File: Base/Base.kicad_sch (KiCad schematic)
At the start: 33 parts, among them J1 USB_C_Receptacle_USB2.0_16P, J10 JST_switch_1, J11 JST_switch_2, J12 Conn_touch_1, J13 Conn_touch_2, J2 JST_battery, J3 JST_header, J4 JST_speaker, J5 JST_debug_swd, J6 JST_debug_serial, J7 Conn_speaker_sd, J8 Conn_speaker_gain, J9 Conn_speaker_gnd, SW1 SW_power, U1 MCP73831-2-OT, U2 MAX98357A

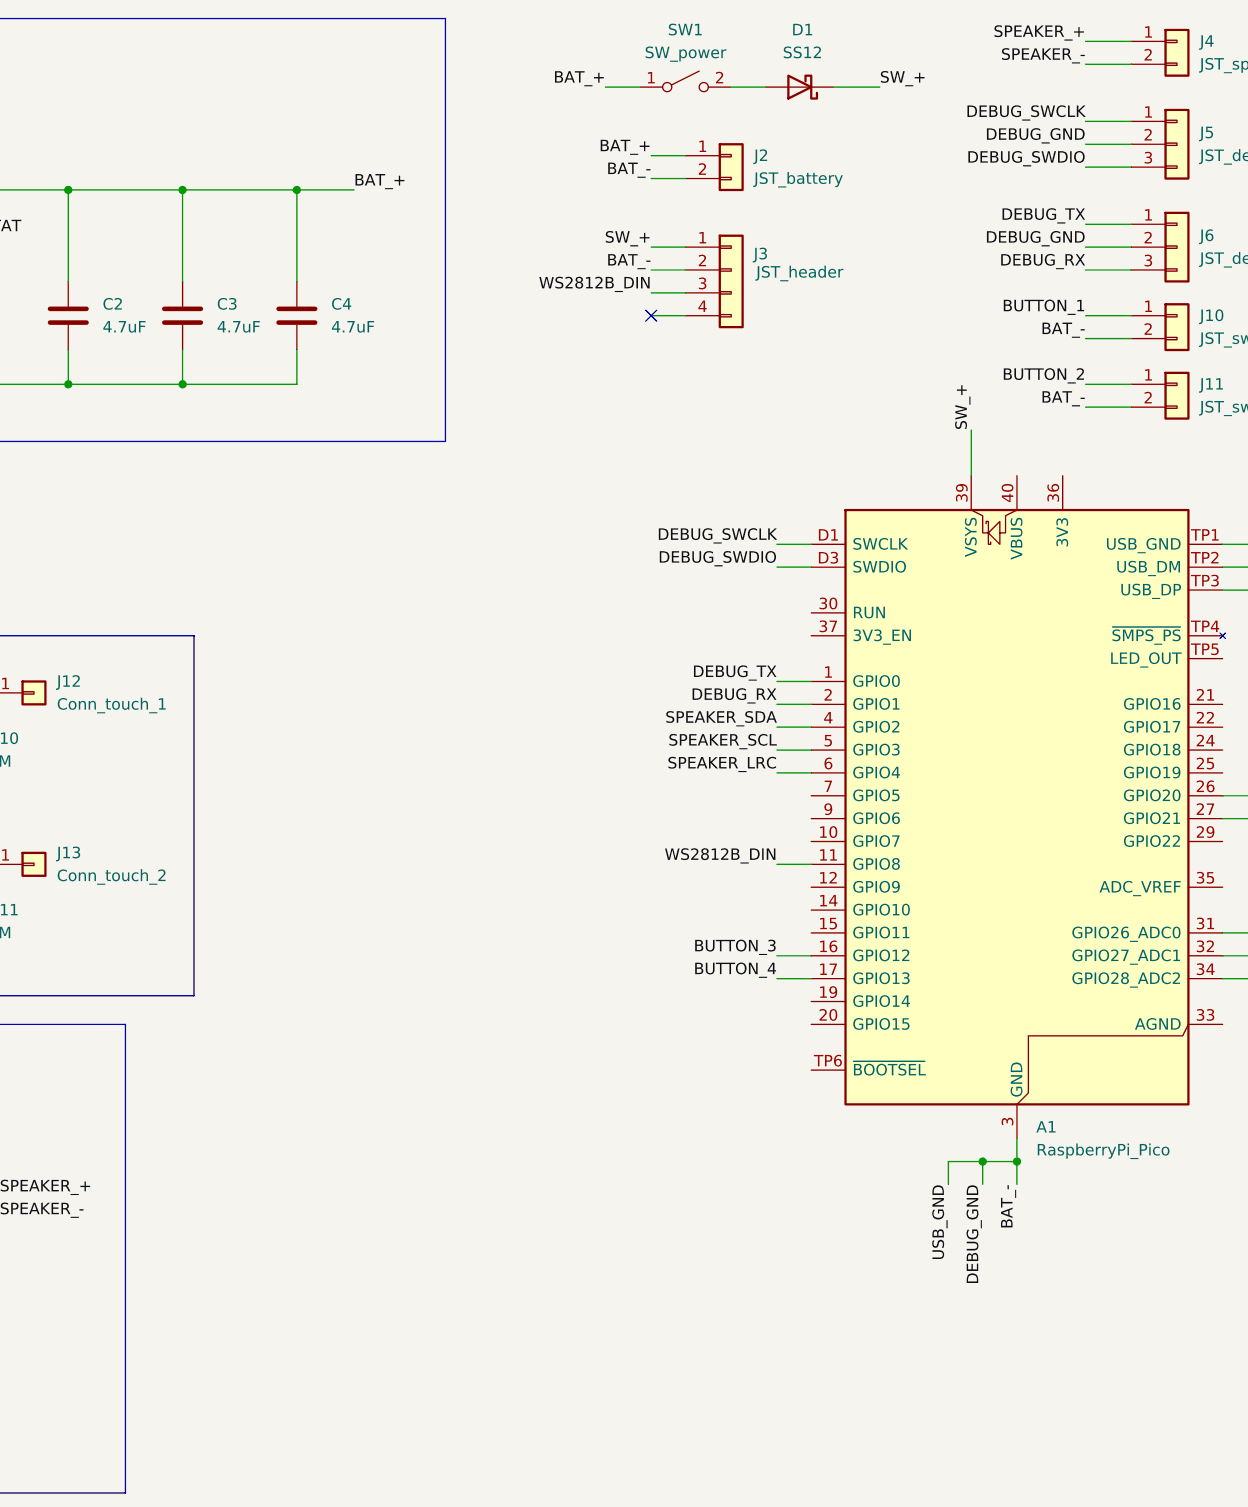
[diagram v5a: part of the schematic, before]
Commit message: Change switch to JST, fix polarity of battery connector, add power transistors for better LED off capability
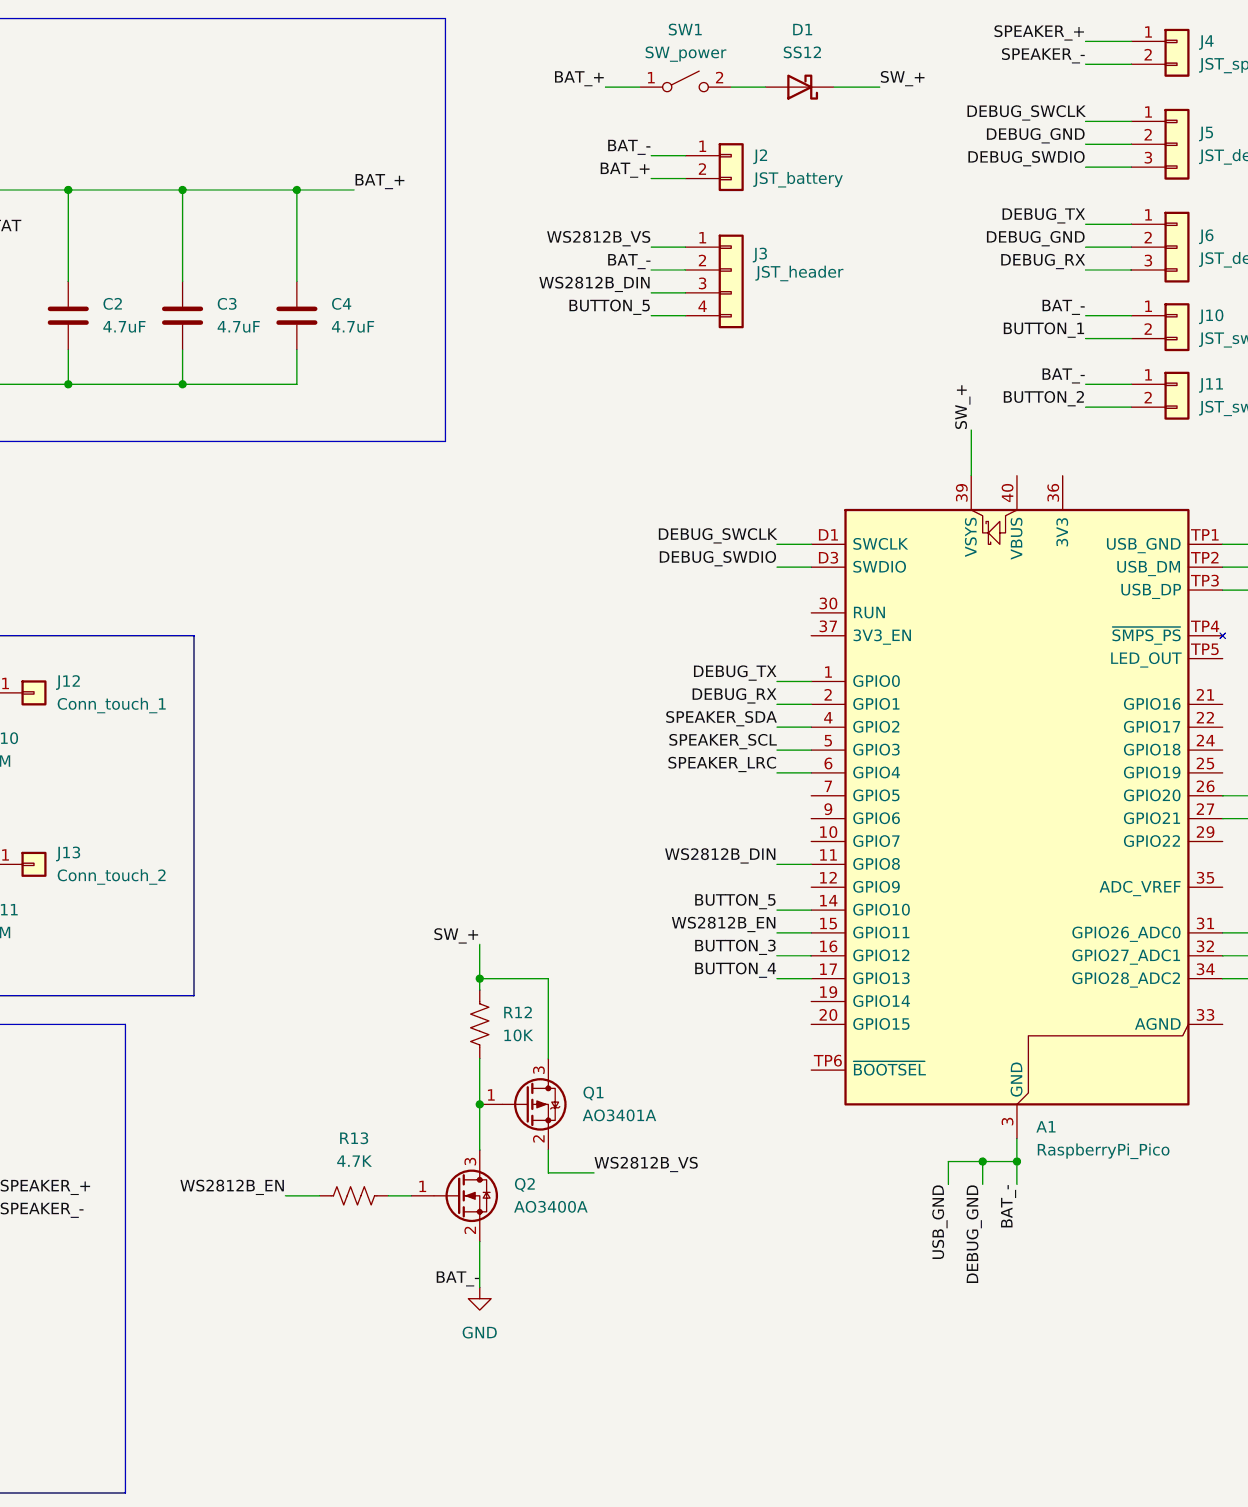
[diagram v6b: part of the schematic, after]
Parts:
- added Q1: AO3401A, Package_TO_SOT_SMD:SOT-23, symbol Transistor_FET:AO3401A
- added Q2: AO3400A, Package_TO_SOT_SMD:SOT-23, symbol Transistor_FET:AO3400A
- added R12: 10K, Resistor_SMD:R_0603_1608Metric_Pad0.98x0.95mm_HandSolder, symbol Device:R_US
- added R13: 4.7K, Resistor_SMD:R_0603_1608Metric_Pad0.98x0.95mm_HandSolder, symbol Device:R_US
- J10, J11: footprint Connector_JST:JST_SH_SM02B-SRSS-TB_1x02-1MP_P1.00mm_Horizontal -> Connector_JST:JST_SH_BM02B-SRSS-TB_1x02-1MP_P1.00mm_Vertical
- J2: footprint Connector_JST:JST_SH_SM02B-SRSS-TB_1x02-1MP_P1.00mm_Horizontal -> Connector_JST:JST_PH_B2B-PH-SM4-TB_1x02-1MP_P2.00mm_Vertical
- J4: footprint Connector_JST:JST_PH_B2B-PH-SM4-TB_1x02-1MP_P2.00mm_Vertical -> Connector_JST:JST_SH_BM02B-SRSS-TB_1x02-1MP_P1.00mm_Vertical
- SW1: footprint Button_Switch_SMD:SW_SPST_B3U-3000P -> Connector_JST:JST_SH_BM02B-SRSS-TB_1x02-1MP_P1.00mm_Vertical
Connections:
- net BAT_+: now also J2.2 (Pin_2); no longer J2.1 (Pin_1)
- net BUTTON_1: now also J10.2 (Pin_2); no longer J10.1 (Pin_1)
- net BUTTON_2: now also J11.2 (Pin_2); no longer J11.1 (Pin_1)
- net SW_+: now also Q1.3 (D), R12.1; no longer J3.1 (Pin_1)
- net BUTTON_5: now reaches A1.14 (GPIO10)
- net BUTTON_5: now also J3.4 (Pin_4)
- net WS2812B_EN: now reaches A1.15 (GPIO11)
- net WS2812B_EN: now also R13.1
- net BAT_- renamed GND
- net GND: now also J10.1 (Pin_1), J11.1 (Pin_1), J2.1 (Pin_1), Q2.2 (S); no longer J10.2 (Pin_2), J11.2 (Pin_2), J2.2 (Pin_2)
- new net: Q1.1 (G), Q2.3 (D), R12.2
- new net: Q2.1 (G), R13.2
- new net WS2812B_VS: J3.1 (Pin_1), Q1.2 (S)
- no-connect marks 4 -> 3

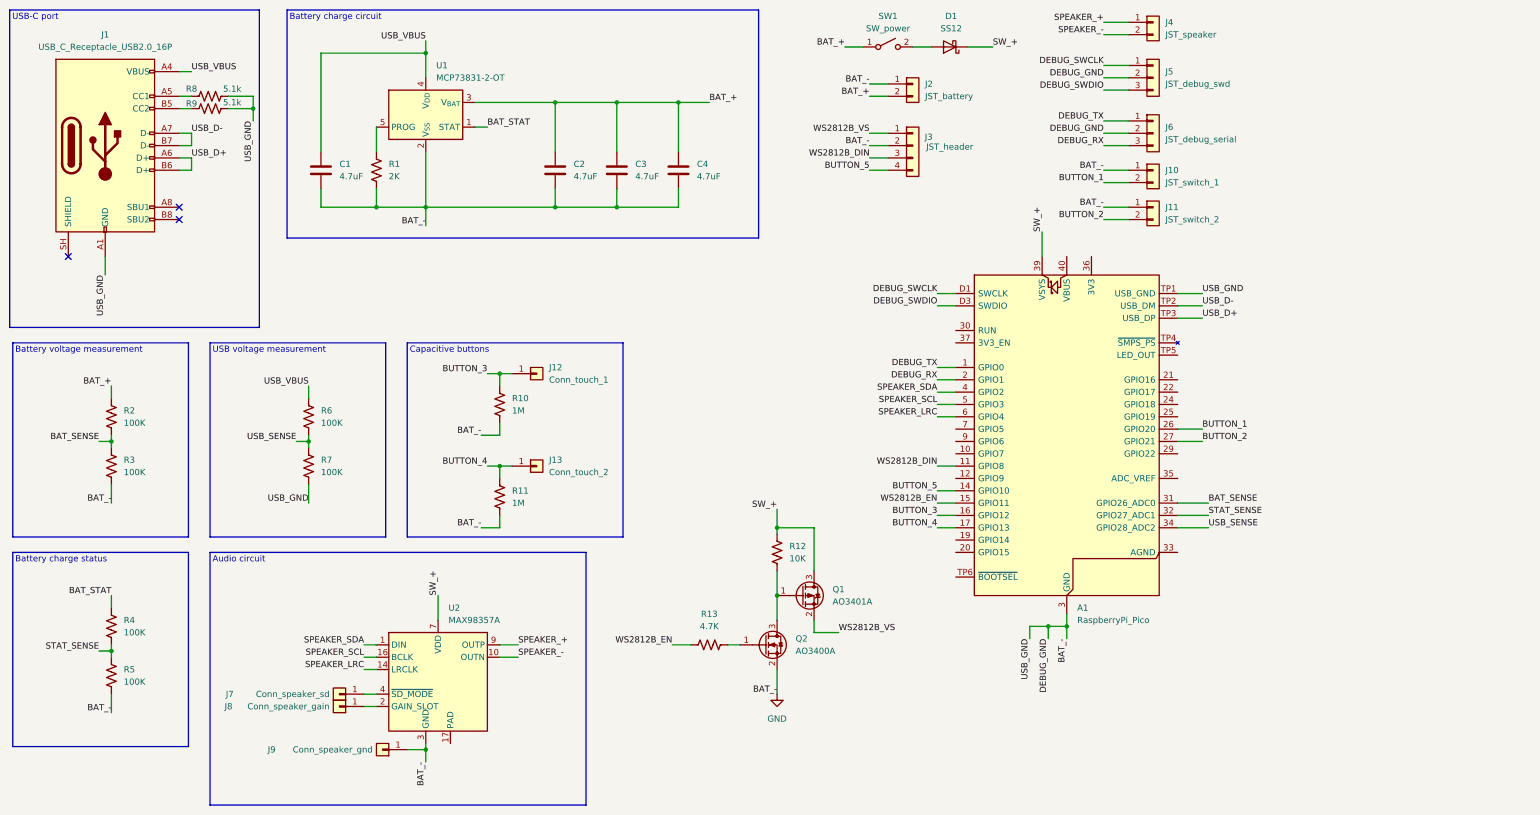
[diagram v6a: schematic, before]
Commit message: Add polarity solder jumpers for batteries that come in RNG polarity
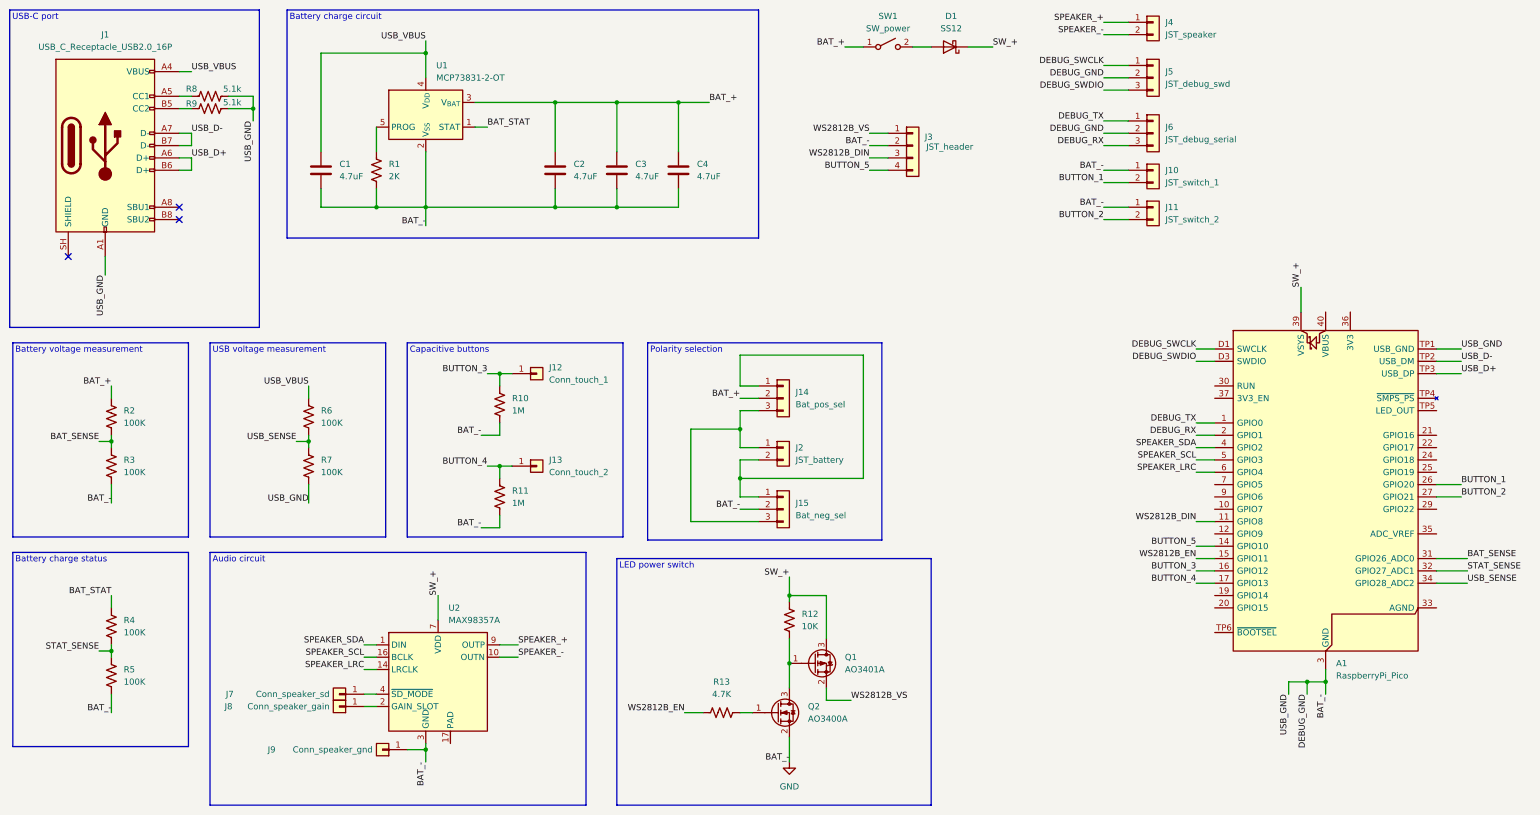
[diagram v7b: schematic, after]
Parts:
- added J14: Bat_pos_sel, Jumper:SolderJumper-3_P2.0mm_Open_TrianglePad1.0x1.5mm_NumberLabels, symbol Connector_Generic:Conn_01x03
- added J15: Bat_neg_sel, Jumper:SolderJumper-3_P2.0mm_Open_TrianglePad1.0x1.5mm_NumberLabels, symbol Connector_Generic:Conn_01x03
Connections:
- net BAT_+: now also J14.2 (Pin_2); no longer J2.2 (Pin_2)
- net GND: now also J15.2 (Pin_2); no longer J2.1 (Pin_1)
- new net: J14.1 (Pin_1), J15.1 (Pin_1), J2.2 (Pin_2)
- new net: J14.3 (Pin_3), J15.3 (Pin_3), J2.1 (Pin_1)
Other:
- note added: "LED power switch"
- note added: "Polarity selection"
- moved on the sheet: A1, J2, Q1, Q2, R12, R13
